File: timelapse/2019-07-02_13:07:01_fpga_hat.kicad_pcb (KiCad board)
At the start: 4 copper layers, 65 x 56.5 mm, 90 parts, among them J1 2x20, J2 AudioJack3, J3 Conn_02x06_Top_Bottom, J4 Conn_02x06_Top_Bottom, J5 Conn_02x06_Top_Bottom, J6 Conn_01x02, SW1 PTS815, SW2 PTS815, SW3 PTS815, SW4 PTS815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

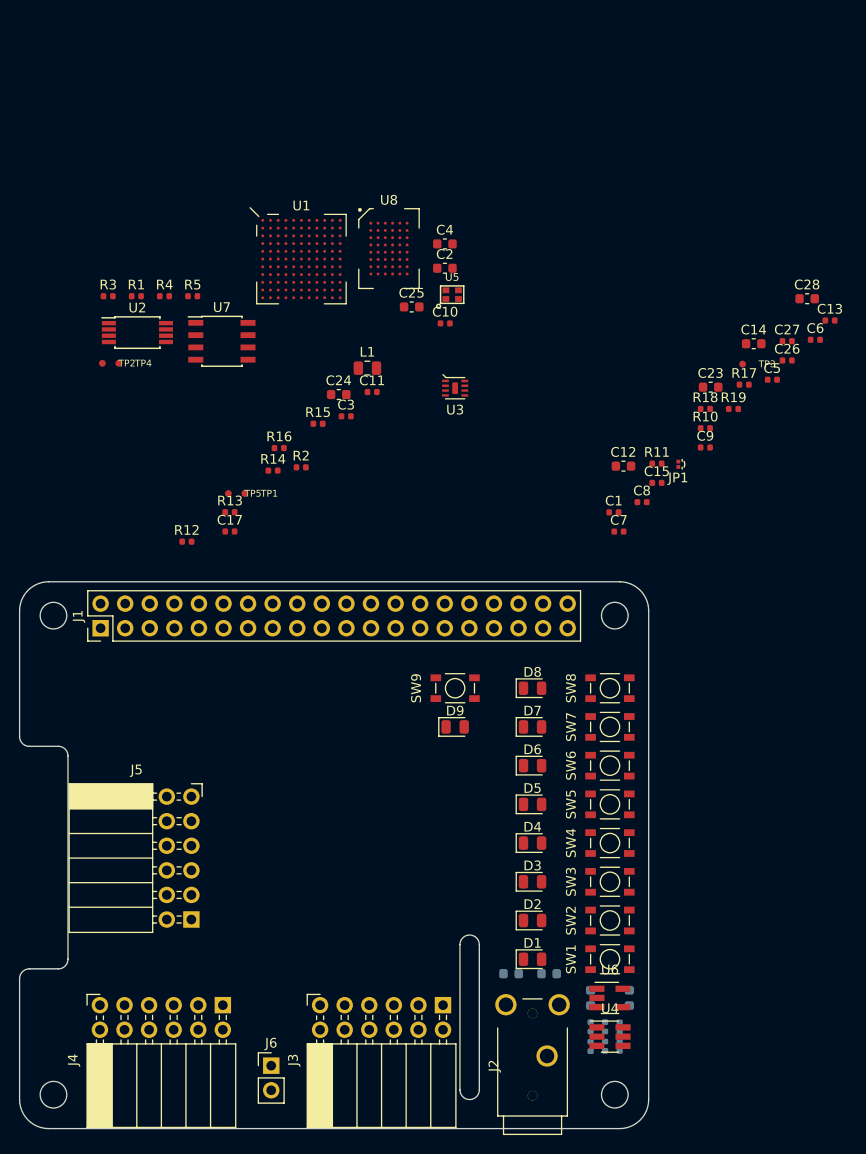
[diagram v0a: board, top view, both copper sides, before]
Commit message: Start placing components
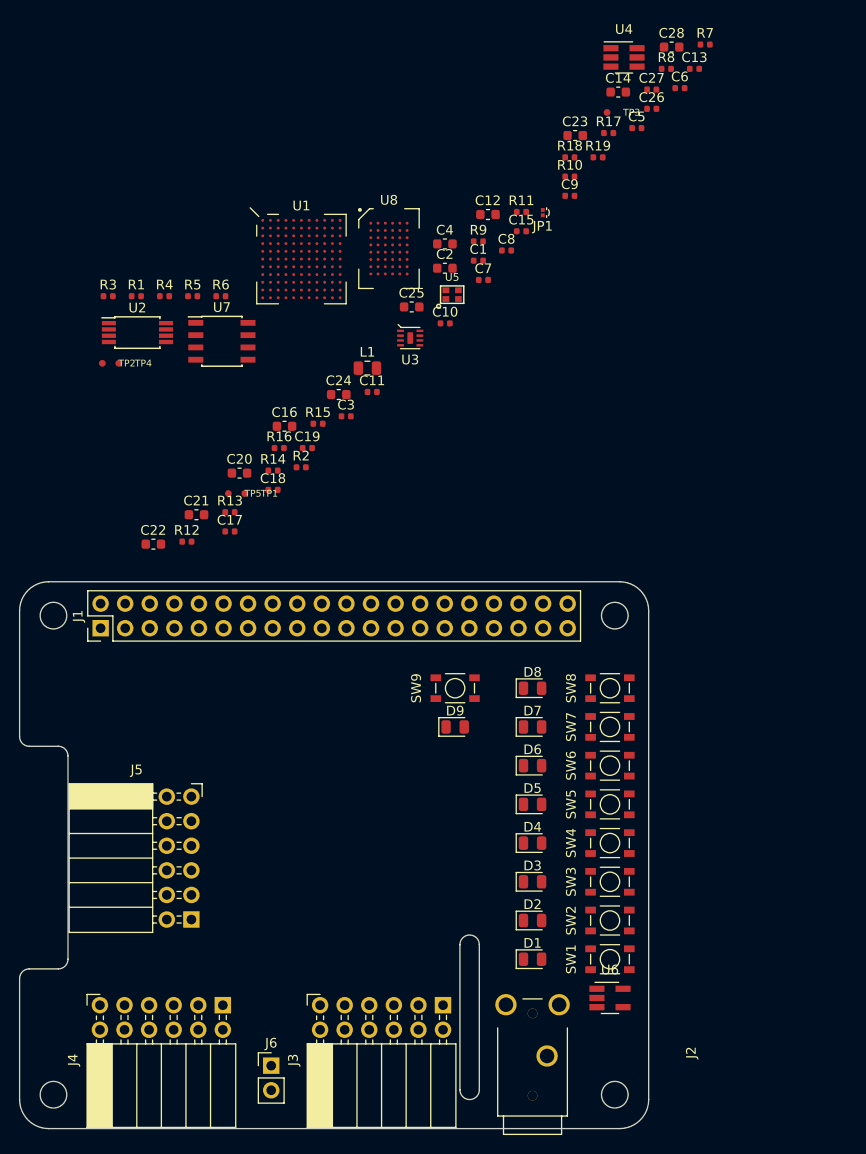
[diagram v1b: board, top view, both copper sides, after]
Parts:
- C16, C18, C19, C20, C21, C22, R6, R7, R8, R9: moved to F.Cu
- moved R7 103.9 mm to (170.8, 24.5), turned to 0 degrees
- moved U4 101.2 mm to (162.4, 25.8)
- moved R8 99.2 mm to (166.8, 27.0), turned to 0 degrees
- moved R6 86.0 mm to (120.8, 50.5), turned to 0 degrees
- moved R9 84.2 mm to (147.4, 44.8), turned to 0 degrees
- moved C19 68.4 mm to (129.7, 66.2), turned to 0 degrees
- moved C22 67.9 mm to (113.8, 76.1), turned to 0 degrees
- moved C16 67.0 mm to (127.4, 63.9), turned to 0 degrees
- moved C18 64.5 mm to (126.2, 70.5), turned to 0 degrees
- moved C20 60.8 mm to (122.7, 68.8)
- moved C21 57.5 mm to (118.3, 73.1)
- moved C12 29.5 mm to (148.4, 42.1)
- moved C26 29.5 mm to (165.3, 31.1)
- moved C6 29.5 mm to (168.2, 29.0)
- moved C1 29.5 mm to (147.4, 46.8)
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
